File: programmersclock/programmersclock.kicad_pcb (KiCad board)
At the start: 2 copper layers, 93 x 70 mm, 22 parts, among them IC1 MCP2200, J3 USB_OTG, SW1 RST, U1 MCP7940N, U2 LM1117-3.3, U3 ESP-12E, Y1 32.768 kHz, Y2 12 MHz

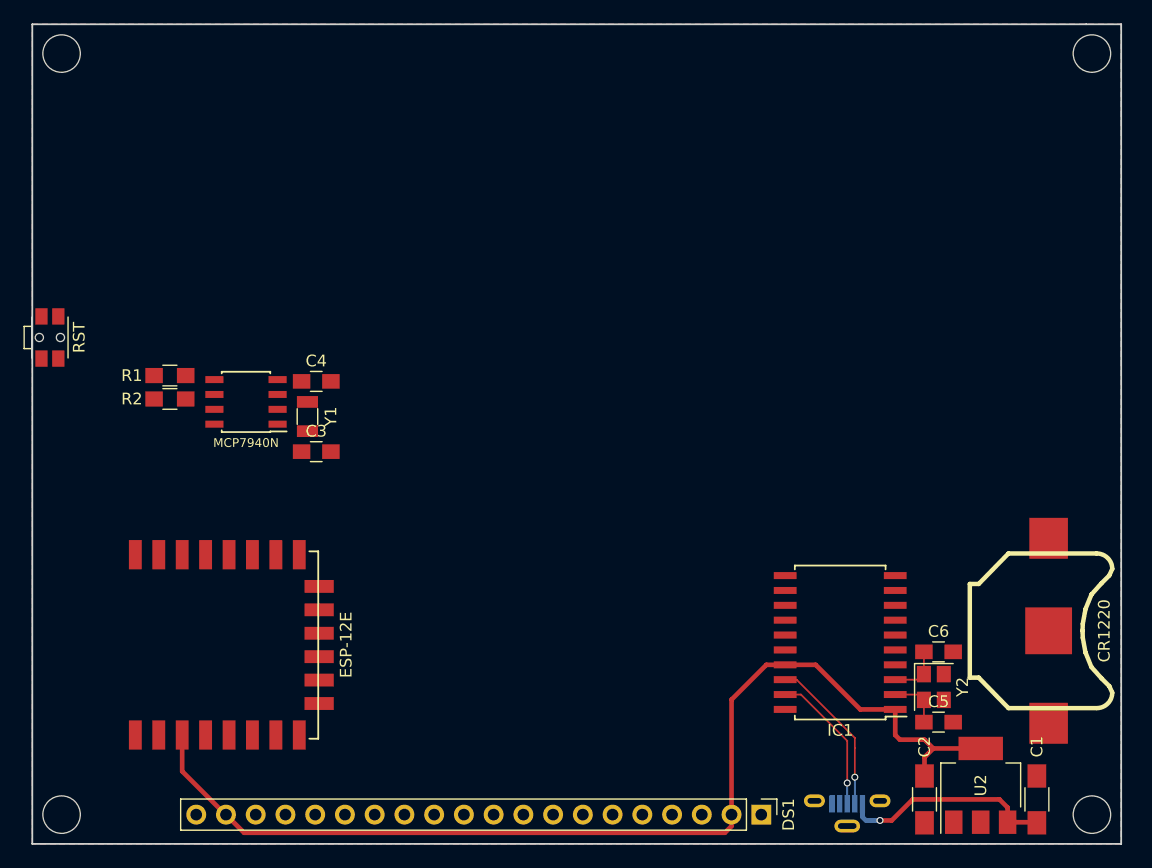
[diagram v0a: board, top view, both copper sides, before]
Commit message: Added recommended battery circuity for the MCP7940N
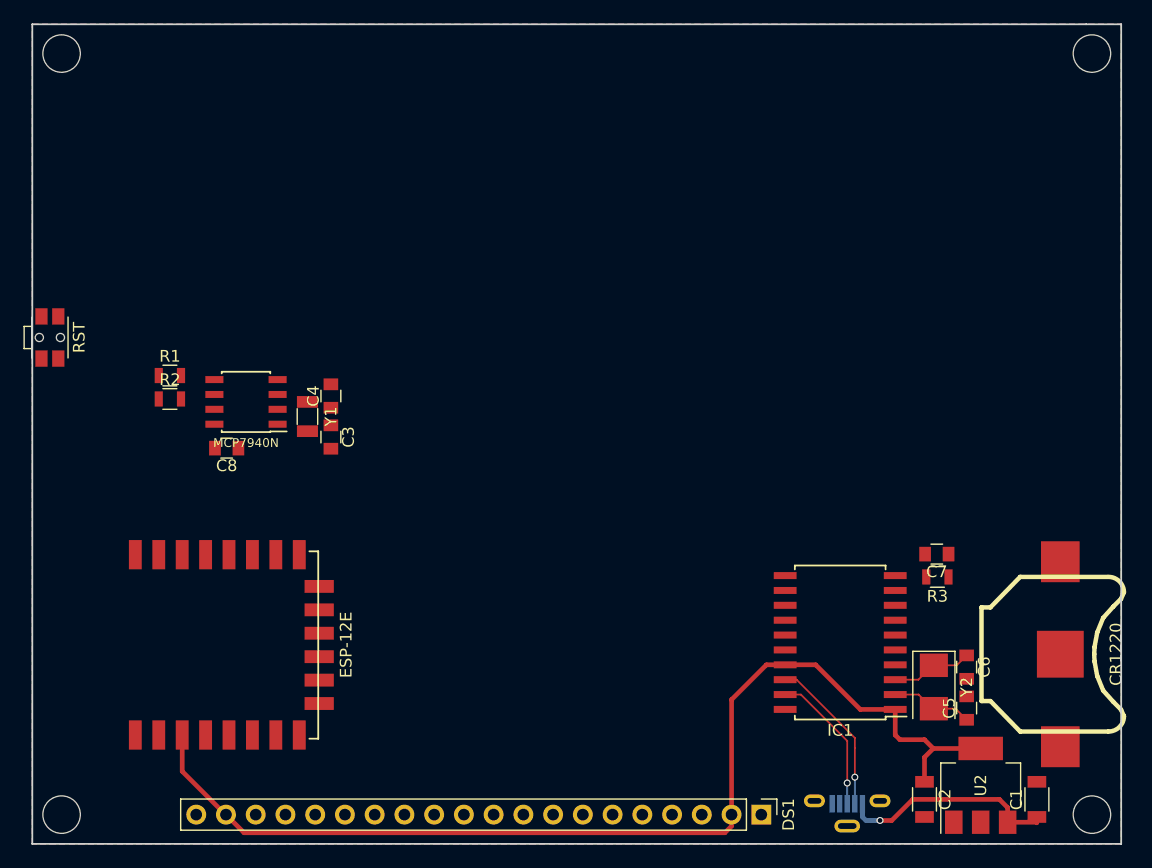
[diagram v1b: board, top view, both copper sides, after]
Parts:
- added C7: 100 pF, Capacitors_SMD:C_0805, F.Cu at (132.2, 135.2)
- added C8: 0.01 uF, Capacitors_SMD:C_0805, F.Cu at (71.6, 126.2)
- added R3: 100k, Resistors_SMD:R_0805, F.Cu at (132.3, 137.2)
- C1, C2: footprint Capacitors_SMD:C_1206_HandSoldering -> Capacitors_SMD:C_1206
- C3, C4, C5, C6: footprint Capacitors_SMD:C_0805_HandSoldering -> Capacitors_SMD:C_0805
- R1, R2: footprint Resistors_SMD:R_0805_HandSoldering -> Resistors_SMD:R_0805
- Y2: footprint Crystals:Crystal_SMD_3225-4pin_3.2x2.5mm -> Crystals:Crystal_SMD_5032-2pin_5.0x3.2mm
- moved C6 2.73 mm to (134.8, 144.9), turned to 270 degrees
- moved C5 2.68 mm to (134.8, 148.4), turned to 90 degrees
- moved BT1 2.24 mm to (142.8, 143.8)
- moved C3 1.77 mm to (80.5, 125.2), turned to 270 degrees
- moved C4 1.77 mm to (80.5, 121.8), turned to 90 degrees
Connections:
- U1 pad 3: Net-(BT1-Pad1) -> +BATT
- U1 pad 8: +3V3 -> Net-(C8-Pad2)
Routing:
- net Net-(C5-Pad1): track 4.54 -> 5.83 mm
- net Net-(C6-Pad1): track 4.55 -> 5.80 mm

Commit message: Replaced battery with CR2032 and general layout rework
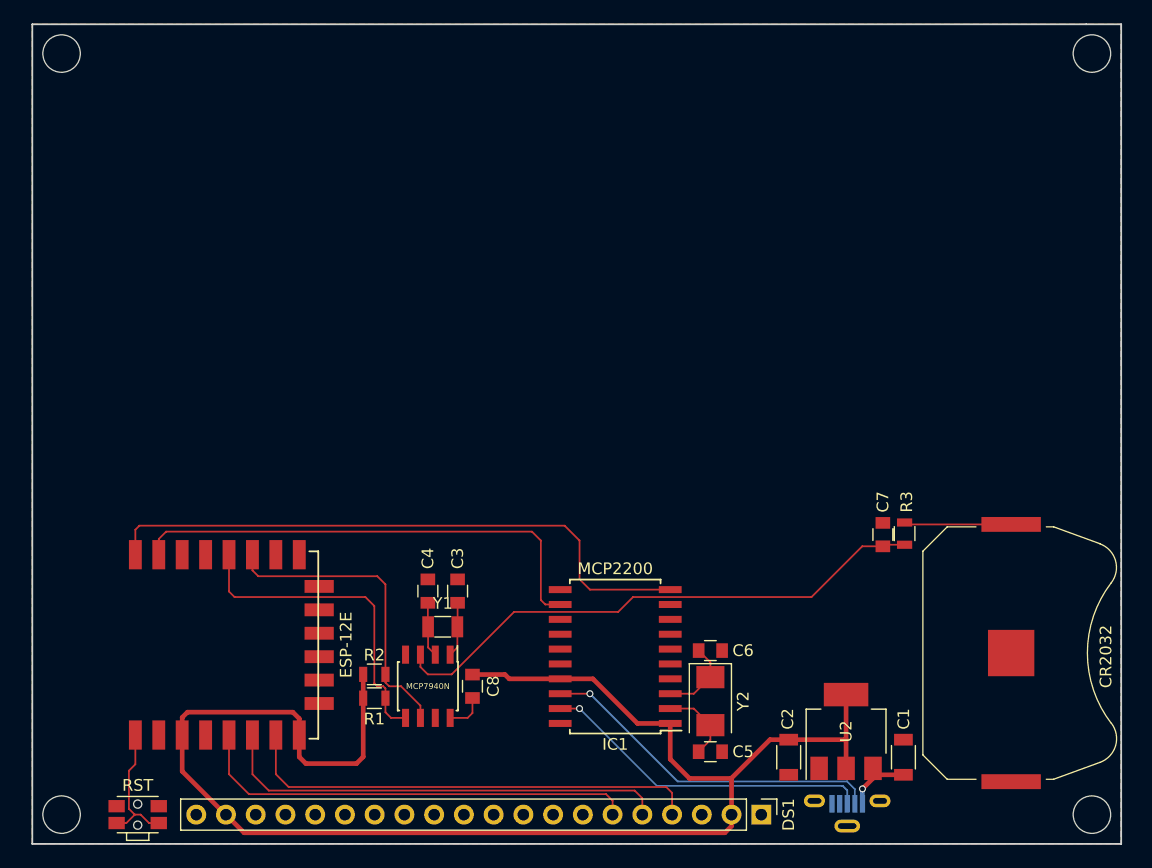
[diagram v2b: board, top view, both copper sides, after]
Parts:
- BT1: value CR1220 -> CR2032; footprint Battery_Holders_extra:BatteryHolder_CoinCell_Keystone_3000 -> Battery_Holders_Clone:Keystone_3034_1x20mm-CoinCell
- Y2: footprint Crystals:Crystal_SMD_5032-2pin_5.0x3.2mm -> Crystals:Crystal_SMD_Abracon_ABM3-2pin_5.0x3.2mm
- moved SW1 41.4 mm to (64.0, 157.5), turned to 0 degrees
- moved R1 32.6 mm to (84.2, 147.6)
- moved R2 29.3 mm to (84.2, 145.5)
- moved C8 29.2 mm to (92.6, 146.5), turned to 270 degrees
- moved U1 28.8 mm to (88.8, 146.5), turned to 270 degrees
- moved C5 22.2 mm to (112.9, 152.1), turned to 0 degrees
- moved C6 21.9 mm to (112.9, 143.5), turned to 0 degrees
- moved Y1 21.4 mm to (90.1, 141.5), turned to 180 degrees
- moved IC1 19.3 mm to (104.8, 144.0)
- moved Y2 19.1 mm to (112.9, 147.8)
- moved C4 18.6 mm to (88.8, 138.4)
- moved C3 17.0 mm to (91.3, 138.4), turned to 90 degrees
- moved U2 12.4 mm to (124.5, 150.4)
- moved C2 12.1 mm to (119.6, 152.6)
- moved C1 12.0 mm to (129.4, 152.6)
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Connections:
- U3 pad 10: Net-(DS1-Pad6) -> Net-(U3-Pad10)
- U3 pad 13: Net-(DS1-Pad5) -> Net-(U3-Pad13)
- U3 pad 14: Net-(DS1-Pad4) -> Net-(U3-Pad14)
- U3 pad 5: Net-(U3-Pad5) -> Net-(DS1-Pad6)
- U3 pad 6: Net-(U3-Pad6) -> Net-(DS1-Pad5)
- U3 pad 7: Net-(U3-Pad7) -> Net-(DS1-Pad4)
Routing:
- net TX: track 0.00 -> 52.9 mm
- net +BATT: track 0.00 -> 47.3 mm
- net RX: track 0.00 -> 42.1 mm
- net Net-(DS1-Pad4): track 0.00 -> 40.4 mm
- net Net-(DS1-Pad5): track 0.00 -> 39.6 mm
- net Net-(DS1-Pad6): track 0.00 -> 38.9 mm
- net +3V3: track 93.3 -> 129.9 mm
- net SDA: track 0.00 -> 27.1 mm
- net SCL: track 0.00 -> 25.7 mm
- net Net-(IC1-Pad19): track 12.3 -> 28.6 mm
- net Net-(IC1-Pad18): track 13.6 -> 29.8 mm
- net +5V: track 18.5 -> 6.23 mm
- net RST: track 0.00 -> 12.1 mm
- net Net-(BT1-Pad1): track 0.00 -> 9.17 mm
- net Net-(C4-Pad1): track 0.00 -> 4.69 mm
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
